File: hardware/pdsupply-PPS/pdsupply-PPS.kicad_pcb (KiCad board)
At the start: 4 copper layers, 50.5 x 37.1 mm, 73 parts, among them IC1 LTM8083EY#PBF, IC2 FPF2895UCX, J1 USB4505-03-0-A_REVA, J2 USB4505-03-0-A_REVA, J3 Screw_Terminal_01x02, U1 FUSB307BMPX, U2 ADUM3160, U3 ACS71240KEXBLT-050U5, U4 STM32L432KCUx

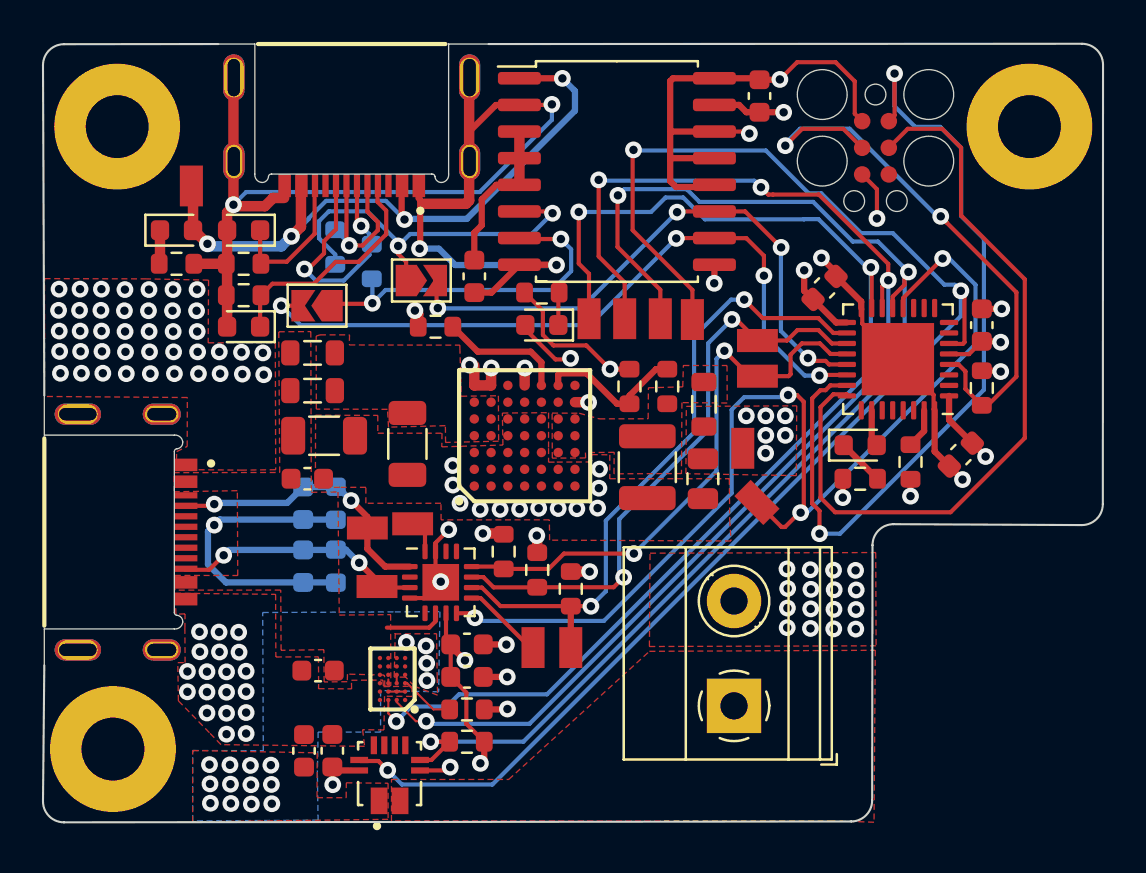
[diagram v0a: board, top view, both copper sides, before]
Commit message: changed Pin A1 on FPF2895 to be connected to GND
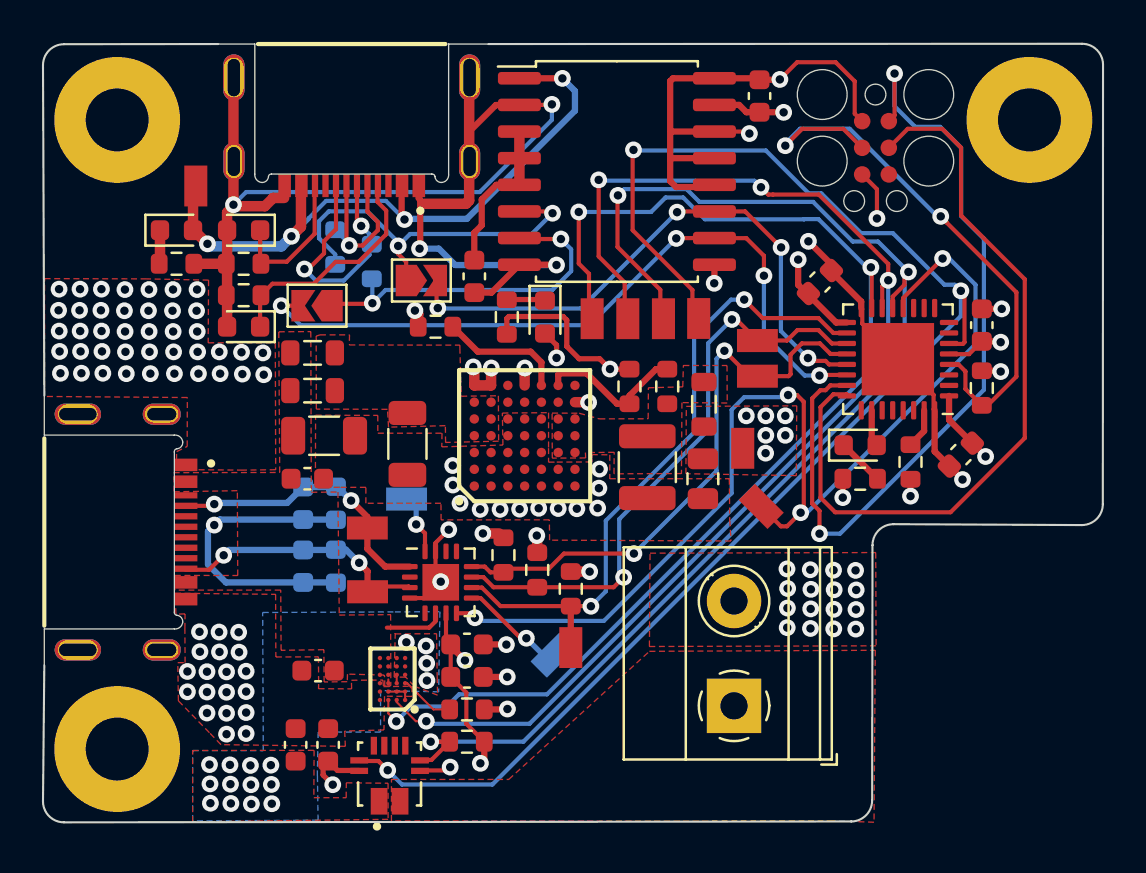
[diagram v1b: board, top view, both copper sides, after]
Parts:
- GPIO1, GPIO2: moved to B.Cu
- moved R14 2.04 mm to (128.8, 95.9), turned to -90 degrees
- moved GPIO1 1.22 mm to (124.1, 104.6), turned to 180 degrees
- moved GPIO2 1.03 mm to (131.1, 112.1), turned to 45 degrees
- moved CC2 0.51 mm to (122.2, 109.0)
- moved C13 0.49 mm to (118.8, 116.3)
- moved D5 0.41 mm to (130.7, 95.9), turned to -90 degrees
- moved C15 0.36 mm to (143.8, 94.3)
- moved C18 0.34 mm to (120.3, 116.3)
- moved H2 0.32 mm to (110.3, 86.5)
- moved H4 0.32 mm to (153.8, 86.5)
- moved Isense1 0.30 mm to (138.0, 96.0)
- moved DBG_N1 0.28 mm to (141.0, 105.0)
- moved +5V1 0.21 mm to (114.0, 89.7)
- moved H1 0.20 mm to (110.3, 116.5)
- moved R4 0.17 mm to (128.7, 107.3)
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- renumbered CC2 to CC1, CC1 to CC2
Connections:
- IC2 pad A1: unconnected-(IC2-PadA1) -> GND
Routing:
- net GND: track 59.7 -> 62.4 mm
- net Net-(GPIO1-Pad1): track 1.50 -> 3.15 mm, vias 0 -> 1
- net Net-(GPIO2-Pad1): track 3.90 -> 5.01 mm, vias 0 -> 1

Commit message: fixed DRC violations
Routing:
- net GND: vias 109 -> 108
